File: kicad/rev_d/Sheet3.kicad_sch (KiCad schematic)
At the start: 112 parts, among them X10 ST-214C, X14 AAFP/AC97 headphones/tapein, X16 PLB1-4I, X17 PLB1-4I, X18 PLB1-4I, X20 PLB1-4I

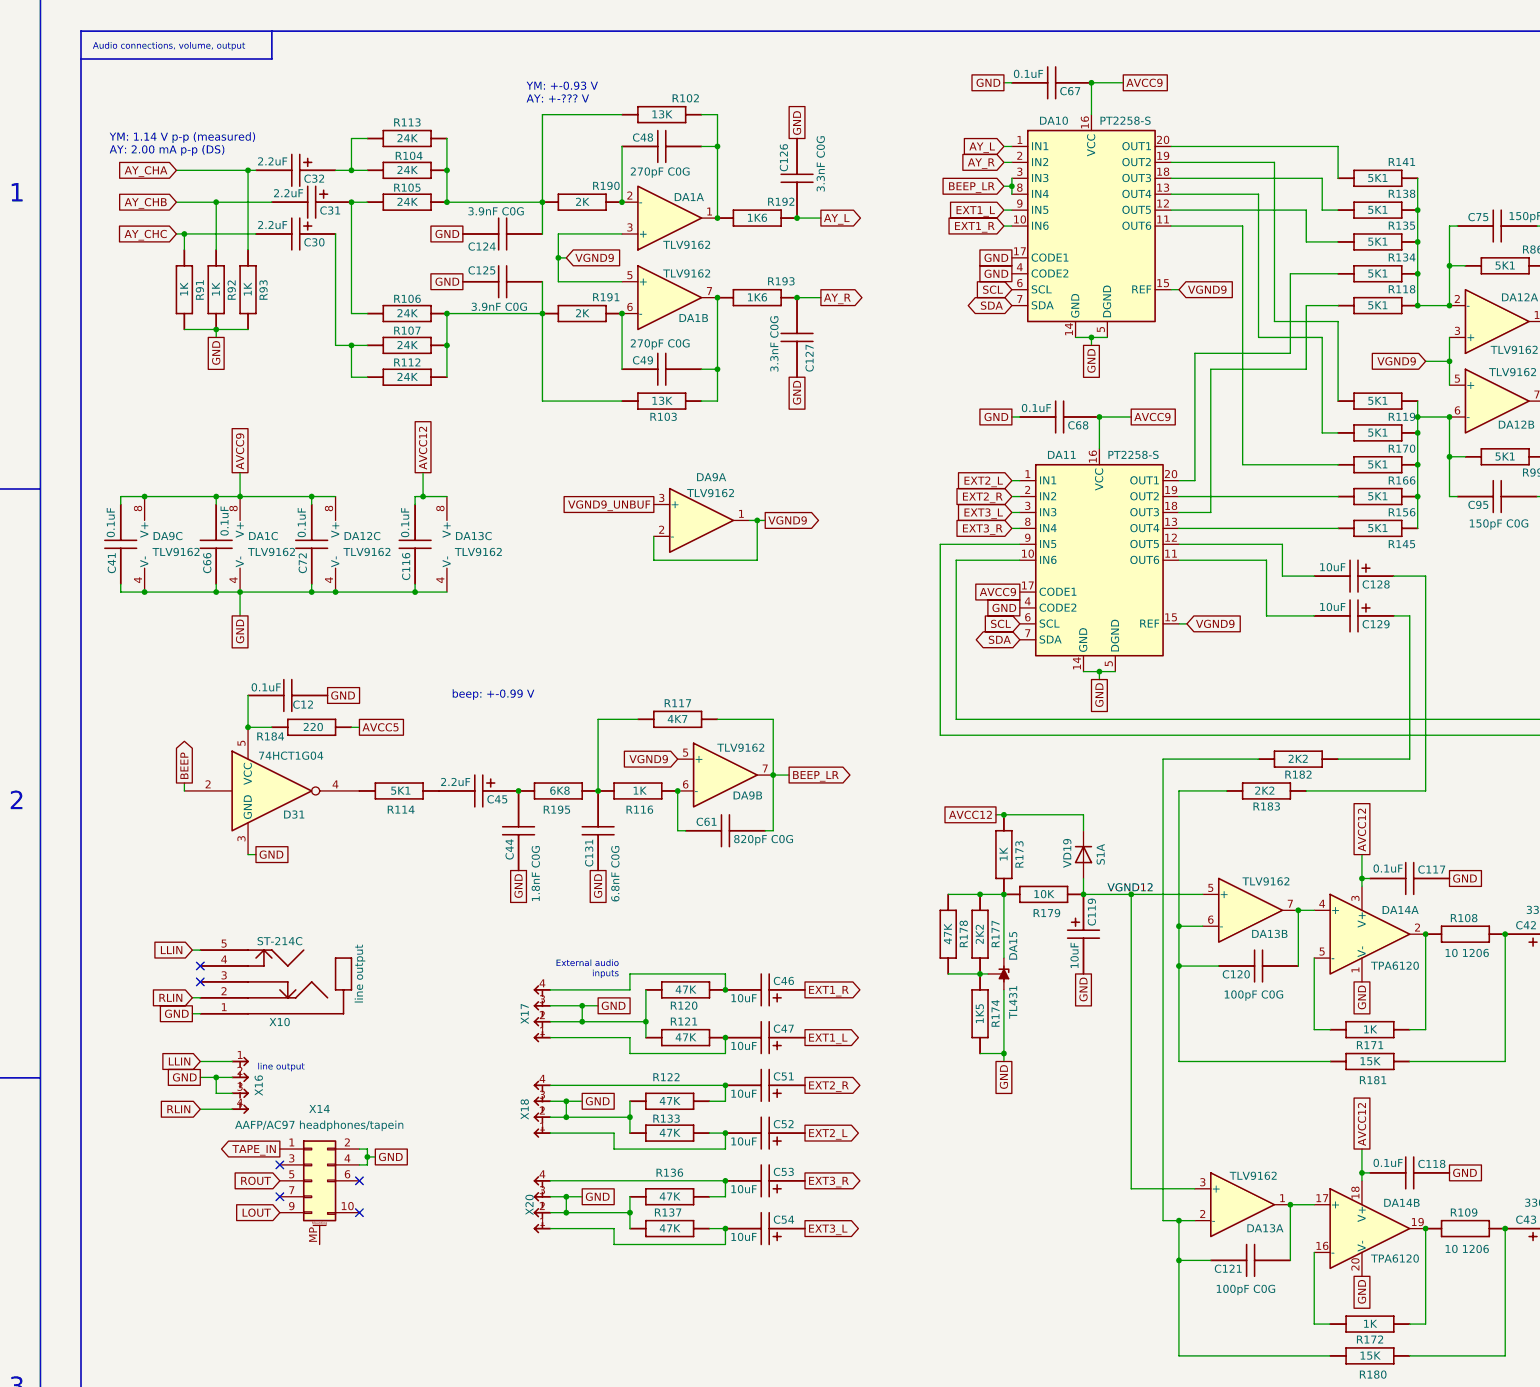
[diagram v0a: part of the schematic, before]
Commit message: pentevo: rev D: video output: use ADV7125 for analog video (WIP)
git-svn-id: svn://localhost/local-pentevo@1276 c6c76956-fad2-4150-a3a9-ea0a427205ba
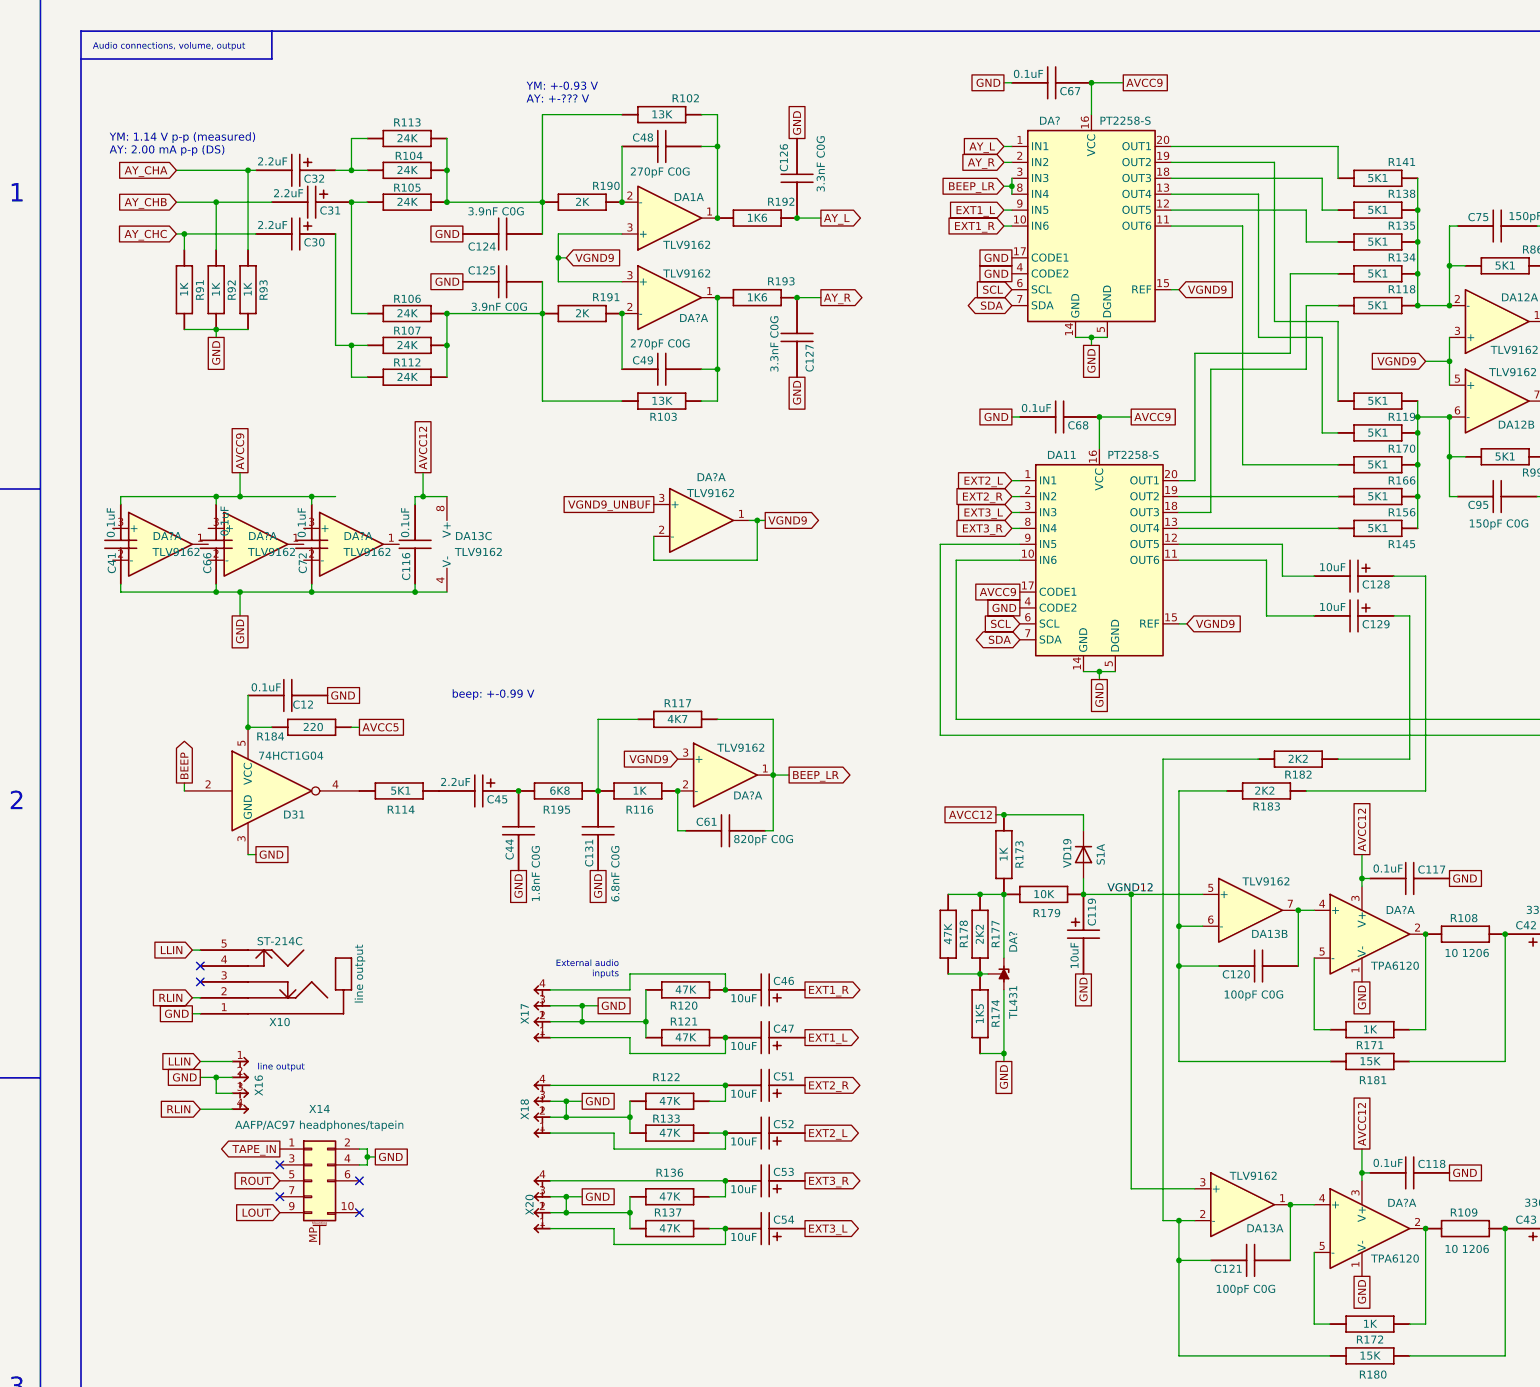
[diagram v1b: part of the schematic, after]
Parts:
- renumbered DA15 to DA?, DA1 to DA?, DA12 to DA?, DA9 to DA?, DA14 to DA?, DA10 to DA?
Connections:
- net AVCC12: now also DA?.3 (V+); no longer DA?.18 (V+)
- net AVCC9: no longer DA?.8 (V+), DA?.8 (V+), DA?.8 (V+)
- net BEEP_LR: now also DA?.1; no longer DA?.7
- net GND: now also DA?.1 (V-); no longer DA?.20 (V-), DA?.4 (V-), DA?.4 (V-), DA?.4 (V-)
- net VGND9: now also DA?.3 (+), DA?.3 (+); no longer DA?.5 (+), DA?.5 (+)
- net at C61.1, R116.1 (i/o): now also DA?.2 (-); no longer DA?.6 (-)
- net at C121.2, DA13.1: now also DA?.4 (+); no longer DA?.17 (+)
- net at C49.1, R191.1 (i/o): now also DA?.2 (-); no longer DA?.6 (-)
- net at C49.2, R103.1 (i/o), R193.2 (i/o1): now also DA?.1; no longer DA?.7
- net at R109.2 (i/o1), R172.1 (i/o): now also DA?.2; no longer DA?.19
- net at R172.2 (i/o1): now also DA?.5 (-); no longer DA?.16 (-)
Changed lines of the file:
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@@
 	)
 	(junction
-		(at 33.02 118.11)
-		(diameter 0)
-		(color 0 0 0 0)
-	)
-	(junction
 		(at 77.47 102.87)
 		(diameter 0)
@@
 	)
 	(junction
-		(at 33.02 102.87)
-		(diameter 0)
-		(color 0 0 0 0)
-	)
-	(junction
 		(at 241.3 81.28)
 		(diameter 0)
@@
 	)
 	(junction
-		(at 63.5 118.11)
-		(diameter 0)
-		(color 0 0 0 0)
-	)
-	(junction
 		(at 182.88 166.37)
 		(diameter 0)
@@
 	(wire
 		(pts
-			(xy 33.02 118.11) (xy 29.21 118.11)
+			(xy 29.21 118.11) (xy 44.45 118.11)
 		)
 		(stroke
@@
 	(wire
 		(pts
-			(xy 59.69 118.11) (xy 63.5 118.11)
+			(xy 59.69 118.11) (xy 76.2 118.11)
 		)
 		(stroke
@@
 	(wire
 		(pts
-			(xy 63.5 118.11) (xy 76.2 118.11)
-		)
-		(stroke
-			(width 0)
-			(type default)
-		)
-	)
-	(wire
-		(pts
 			(xy 96.52 41.91) (xy 96.52 55.88)
 		)
@@
 	(wire
 		(pts
-			(xy 33.02 118.11) (xy 44.45 118.11)
-		)
-		(stroke
-			(width 0)
-			(type default)
-		)
-	)
-	(wire
-		(pts
 			(xy 220.98 52.07) (xy 220.98 57.15)
 		)
@@
 	(wire
 		(pts
-			(xy 33.02 102.87) (xy 44.45 102.87)
-		)
-		(stroke
-			(width 0)
-			(type default)
-		)
-	)
-	(wire
-		(pts
 			(xy 203.2 105.41) (xy 198.12 105.41)
 		)
@@
 	(wire
 		(pts
-			(xy 29.21 102.87) (xy 33.02 102.87)
+			(xy 29.21 102.87) (xy 44.45 102.87)
 		)
 		(stroke
@@
 		(on_board yes)
 		(dnp no)
-		(property "Reference" "DA15"
+		(property "Reference" "DA?"
 			(at 171.704 172.212 0)
 			(effects
@@
 		(pin "3"
 		)
+		(instances
+			(project "eva"
+				(path "/ab605654-a730-497b-9e09-9b351f74b935/d12fc3f7-914a-41f9-b933-632d1b3e89f3"
+					(reference "DA?")
+					(unit 1)
+				)
+			)
+		)
 	)
 	(symbol
 		(lib_id "eva-altium-import:TLC072")
 		(at 116.84 71.12 0)
-		(unit 2)
+		(unit 1)
 		(exclude_from_sim no)
 		(in_bom yes)
 		(on_board yes)
 		(dnp no)
-		(property "Reference" "DA1"
+		(property "Reference" "DA?"
 			(at 120.65 74.422 0)
 			(effects
@@
 		(pin "3"
 		)
+		(instances
+			(project "eva"
+				(path "/ab605654-a730-497b-9e09-9b351f74b935/d12fc3f7-914a-41f9-b933-632d1b3e89f3"
+					(reference "DA?")
+					(unit 1)
+				)
+			)
+		)
 	)
 	(symbol
@@
 		(lib_id "eva-altium-import:TLC072")
 		(at 66.04 110.49 0)
-		(unit 3)
+		(unit 1)
 		(exclude_from_sim no)
 		(in_bom yes)
@@
 		(dnp no)
 		(fields_autoplaced yes)
-		(property "Reference" "DA12"
+		(property "Reference" "DA?"
 			(at 64.77 109.2199 0)
 			(effects
@@
 		(pin "7"
 		)
+		(instances
+			(project "eva"
+				(path "/ab605654-a730-497b-9e09-9b351f74b935/d12fc3f7-914a-41f9-b933-632d1b3e89f3"
+					(reference "DA?")
+					(unit 1)
+				)
+			)
+		)
 	)
 	(symbol
@@
 		(lib_id "eva-altium-import:TLC072")
 		(at 50.8 110.49 0)
-		(unit 3)
+		(unit 1)
 		(exclude_from_sim no)
 		(in_bom yes)
@@
 		(dnp no)
 		(fields_autoplaced yes)
-		(property "Reference" "DA1"
+		(property "Reference" "DA?"
 			(at 49.53 109.2199 0)
 			(effects
@@
 		(pin "3"
 		)
+		(instances
+			(project "eva"
+				(path "/ab605654-a730-497b-9e09-9b351f74b935/d12fc3f7-914a-41f9-b933-632d1b3e89f3"
+					(reference "DA?")
+					(unit 1)
+				)
+			)
+		)
 	)
 	(symbol
@@
 		(on_board yes)
 		(dnp no)
-		(property "Reference" "DA9"
+		(property "Reference" "DA?"
 			(at 123.444 99.822 0)
 			(effects
@@
 		(pin "2"
 		)
+		(instances
+			(project "eva"
+				(path "/ab605654-a730-497b-9e09-9b351f74b935/d12fc3f7-914a-41f9-b933-632d1b3e89f3"
+					(reference "DA?")
+					(unit 1)
+				)
+			)
+		)
 	)
 	(symbol
@@
 		(lib_id "eva-altium-import:TPA6120")
 		(at 229.87 219.71 0)
-		(unit 2)
+		(unit 1)
 		(exclude_from_sim no)
 		(in_bom yes)
 		(on_board yes)
 		(dnp no)
-		(property "Reference" "DA14"
+		(property "Reference" "DA?"
 			(at 233.68 215.646 0)
 			(effects
@@
 		(pin "16"
 		)
+		(instances
+			(project "eva"
+				(path "/ab605654-a730-497b-9e09-9b351f74b935/d12fc3f7-914a-41f9-b933-632d1b3e89f3"
+					(reference "DA?")
+					(unit 1)
+				)
+			)
+		)
 	)
 	(symbol
@@
 		(lib_id "eva-altium-import:TLC072")
 		(at 35.56 110.49 0)
-		(unit 3)
+		(unit 1)
 		(exclude_from_sim no)
 		(in_bom yes)
@@
 		(dnp no)
 		(fields_autoplaced yes)
-		(property "Reference" "DA9"
+		(property "Reference" "DA?"
 			(at 34.29 109.2199 0)
 			(effects
@@
 		(pin "2"
 		)
+		(instances
+			(project "eva"
+				(path "/ab605654-a730-497b-9e09-9b351f74b935/d12fc3f7-914a-41f9-b933-632d1b3e89f3"
+					(reference "DA?")
+					(unit 1)
+				)
+			)
+		)
 	)
 	(symbol
@@
 		(lib_id "eva-altium-import:TLC072")
 		(at 125.73 147.32 0)
-		(unit 2)
+		(unit 1)
 		(exclude_from_sim no)
 		(in_bom yes)
 		(on_board yes)
 		(dnp no)
-		(property "Reference" "DA9"
+		(property "Reference" "DA?"
 			(at 129.286 150.622 0)
 			(effects
@@
 		(pin "2"
 		)
+		(instances
+			(project "eva"
+				(path "/ab605654-a730-497b-9e09-9b351f74b935/d12fc3f7-914a-41f9-b933-632d1b3e89f3"
+					(reference "DA?")
+					(unit 1)
+				)
+			)
+		)
 	)
 	(symbol
@@
 		(on_board yes)
 		(dnp no)
-		(property "Reference" "DA10"
+		(property "Reference" "DA?"
 			(at 175.768 42.926 0)
 			(effects
@@
 		(pin "5"
 		)
+		(instances
+			(project "eva"
+				(path "/ab605654-a730-497b-9e09-9b351f74b935/d12fc3f7-914a-41f9-b933-632d1b3e89f3"
+					(reference "DA?")
+					(unit 1)
+				)
+			)
+		)
 	)
 	(symbol
@@
 		(on_board yes)
 		(dnp no)
-		(property "Reference" "DA14"
+		(property "Reference" "DA?"
 			(at 233.426 168.91 0)
 			(effects
@@
 		(pin "16"
 		)
+		(instances
+			(project "eva"
+				(path "/ab605654-a730-497b-9e09-9b351f74b935/d12fc3f7-914a-41f9-b933-632d1b3e89f3"
+					(reference "DA?")
+					(unit 1)
+				)
+			)
+		)
 	)
